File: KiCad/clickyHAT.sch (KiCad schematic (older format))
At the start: 16 parts, among them J1 Raspberry_Pi_2_3, Q1 BS170, SW1 SW_Push, SW2 SW_Push, SW3 SW_Push, SW4 SW_Push

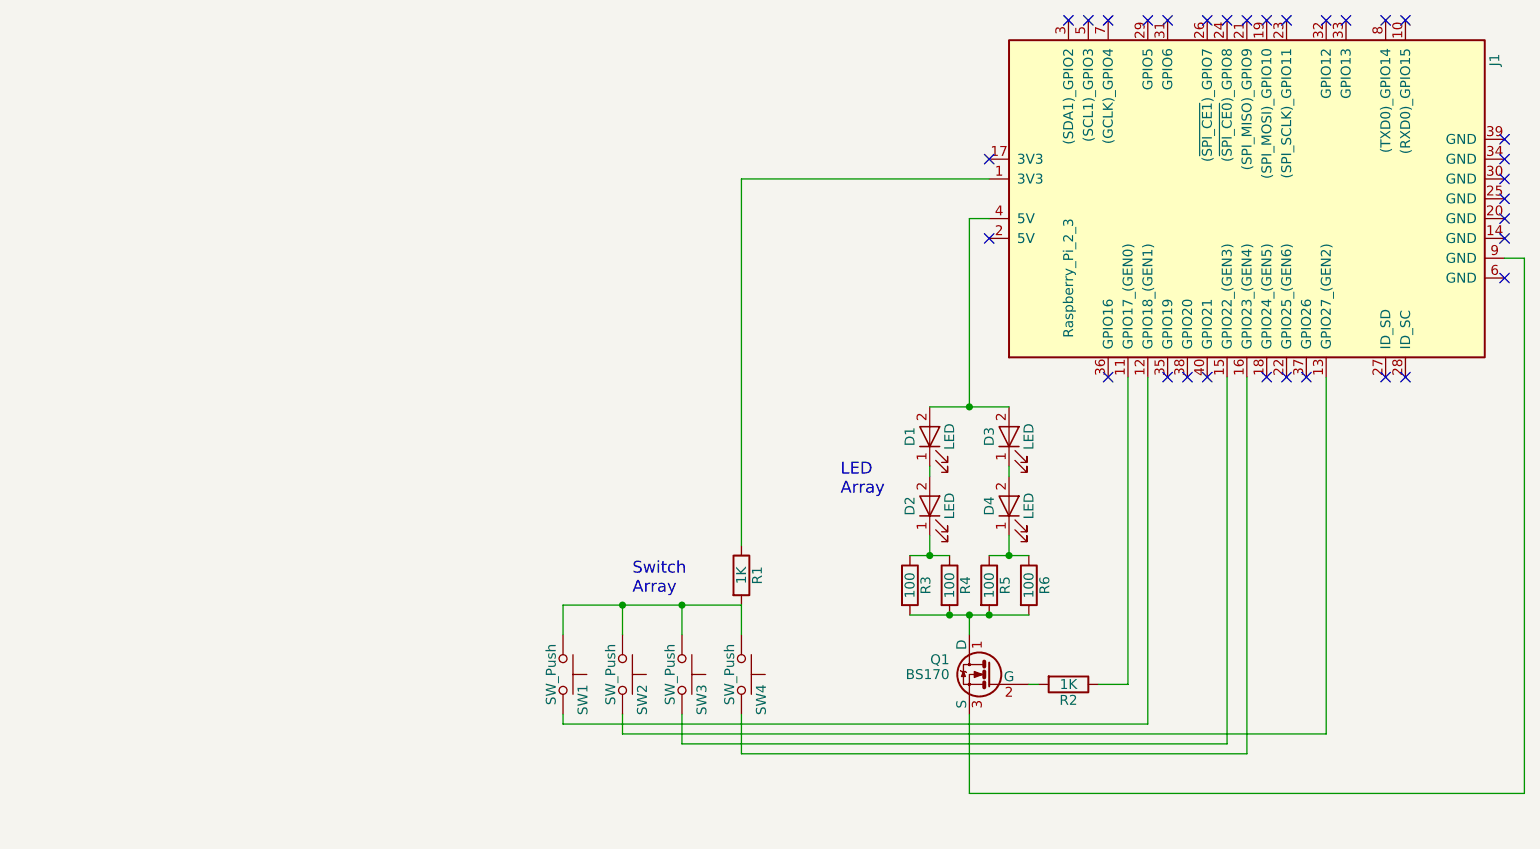
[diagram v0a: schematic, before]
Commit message: Updated board design
removed copper fill, updated gerbers are included
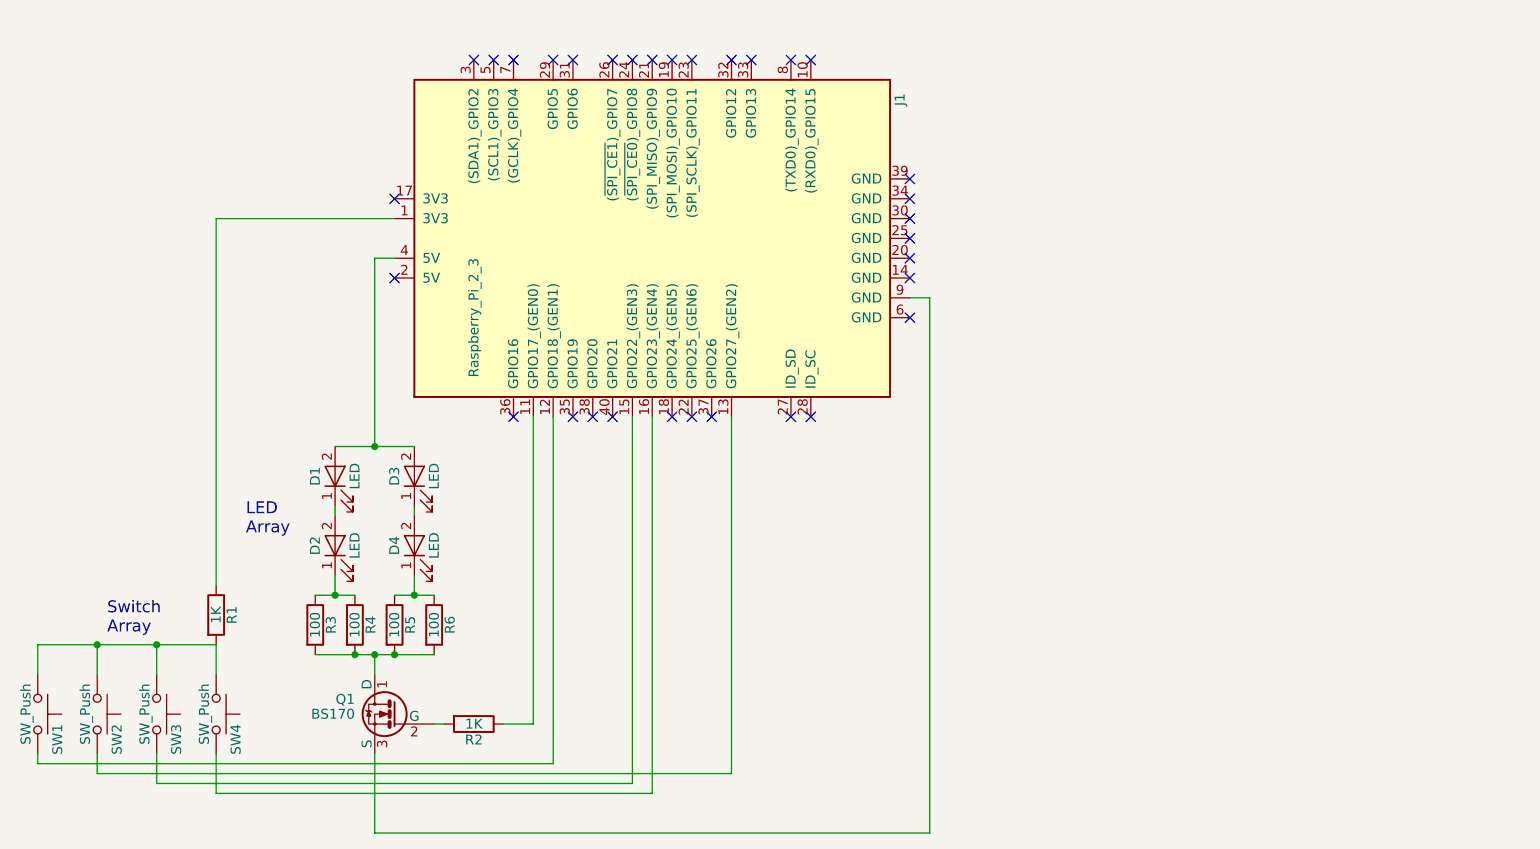
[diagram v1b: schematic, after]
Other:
- moved on the sheet: D1, D2, D3, D4, J1, Q1, R1, R2, R3, R4, R5, R6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

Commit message: Revision 1.1
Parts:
- R3: renamed from R4; value 100 -> 150
- R4: renamed from R3; value 100 -> 150
- R5: renamed from R6; value 100 -> 150
- R6: renamed from R5; value 100 -> 150
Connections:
- net at D1.2 (A), D3.2 (A), J1.4 (5V): now also D2.2 (A), D4.2 (A)
- net at D1.1 (K): now also R4.1; no longer D2.2 (A)
- net at D2.1 (K), R3.1: no longer R4.1
- net at D3.1 (K): now also R6.1; no longer D4.2 (A)
- net at D4.1 (K), R5.1: no longer R6.1
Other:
- moved on the sheet: D1, D2, D3, D4, J1, Q1, R1, R2, R3, R4, R5, R6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

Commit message: Documentation updated
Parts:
- renumbered R5 to R3, R6 to R4, R3 to R5, R4 to R6
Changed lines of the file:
@@
 Rev "1.1"
 Comp ""
-Comment1 ""
+Comment1 "• LEDs are now all parallel to each other (allows a forward voltage of >2.5V)"
 Comment2 ""
 Comment3 ""
@@
 $EndComp
 $Comp
-L R R4
+L R R6
 U 1 1 596FEDB1
 P 1900 4450
-F 0 "R4" V 1980 4450 50  0000 C CNN
+F 0 "R6" V 1980 4450 50  0000 C CNN
 F 1 "150" V 1900 4450 50  0000 C CNN
 F 2 "Resistors_THT:R_Axial_DIN0207_L6.3mm_D2.5mm_P7.62mm_Horizontal" V 1830 4450 50  0001 C CNN
@@
 $EndComp
 $Comp
-L R R3
+L R R5
 U 1 1 596FF538
 P 2200 4450
-F 0 "R3" V 2280 4450 50  0000 C CNN
+F 0 "R5" V 2280 4450 50  0000 C CNN
 F 1 "150" V 2200 4450 50  0000 C CNN
 F 2 "Resistors_THT:R_Axial_DIN0207_L6.3mm_D2.5mm_P7.62mm_Horizontal" V 2130 4450 50  0001 C CNN
@@
 $EndComp
 $Comp
-L R R6
+L R R4
 U 1 1 596FF58B
 P 2500 4450
-F 0 "R6" V 2580 4450 50  0000 C CNN
+F 0 "R4" V 2580 4450 50  0000 C CNN
 F 1 "150" V 2500 4450 50  0000 C CNN
 F 2 "Resistors_THT:R_Axial_DIN0207_L6.3mm_D2.5mm_P7.62mm_Horizontal" V 2430 4450 50  0001 C CNN
@@
 $EndComp
 $Comp
-L R R5
+L R R3
 U 1 1 596FF5DF
 P 2800 4450
-F 0 "R5" V 2880 4450 50  0000 C CNN
+F 0 "R3" V 2880 4450 50  0000 C CNN
 F 1 "150" V 2800 4450 50  0000 C CNN
 F 2 "Resistors_THT:R_Axial_DIN0207_L6.3mm_D2.5mm_P7.62mm_Horizontal" V 2730 4450 50  0001 C CNN
